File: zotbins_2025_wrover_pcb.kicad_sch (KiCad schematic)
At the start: 40 parts, among them J1 Conn_01x28_Pin, J2 DCJ200-10-A-XX-K_REVA, J3 HC-SR04_Screw_Terminal_01x04, J4 HX711_Screw_Terminal_01x05, J5 Main_Servo_Screw_Terminal_01x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, J6 Conn_01x30_Pin, J7 SG_Servo_Screw_Terminal_01x03, J8 BB_Receiver_Screw_Terminal_01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, J9 BB_Transmitter_Screw_Terminal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, U1 LM350_TO220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

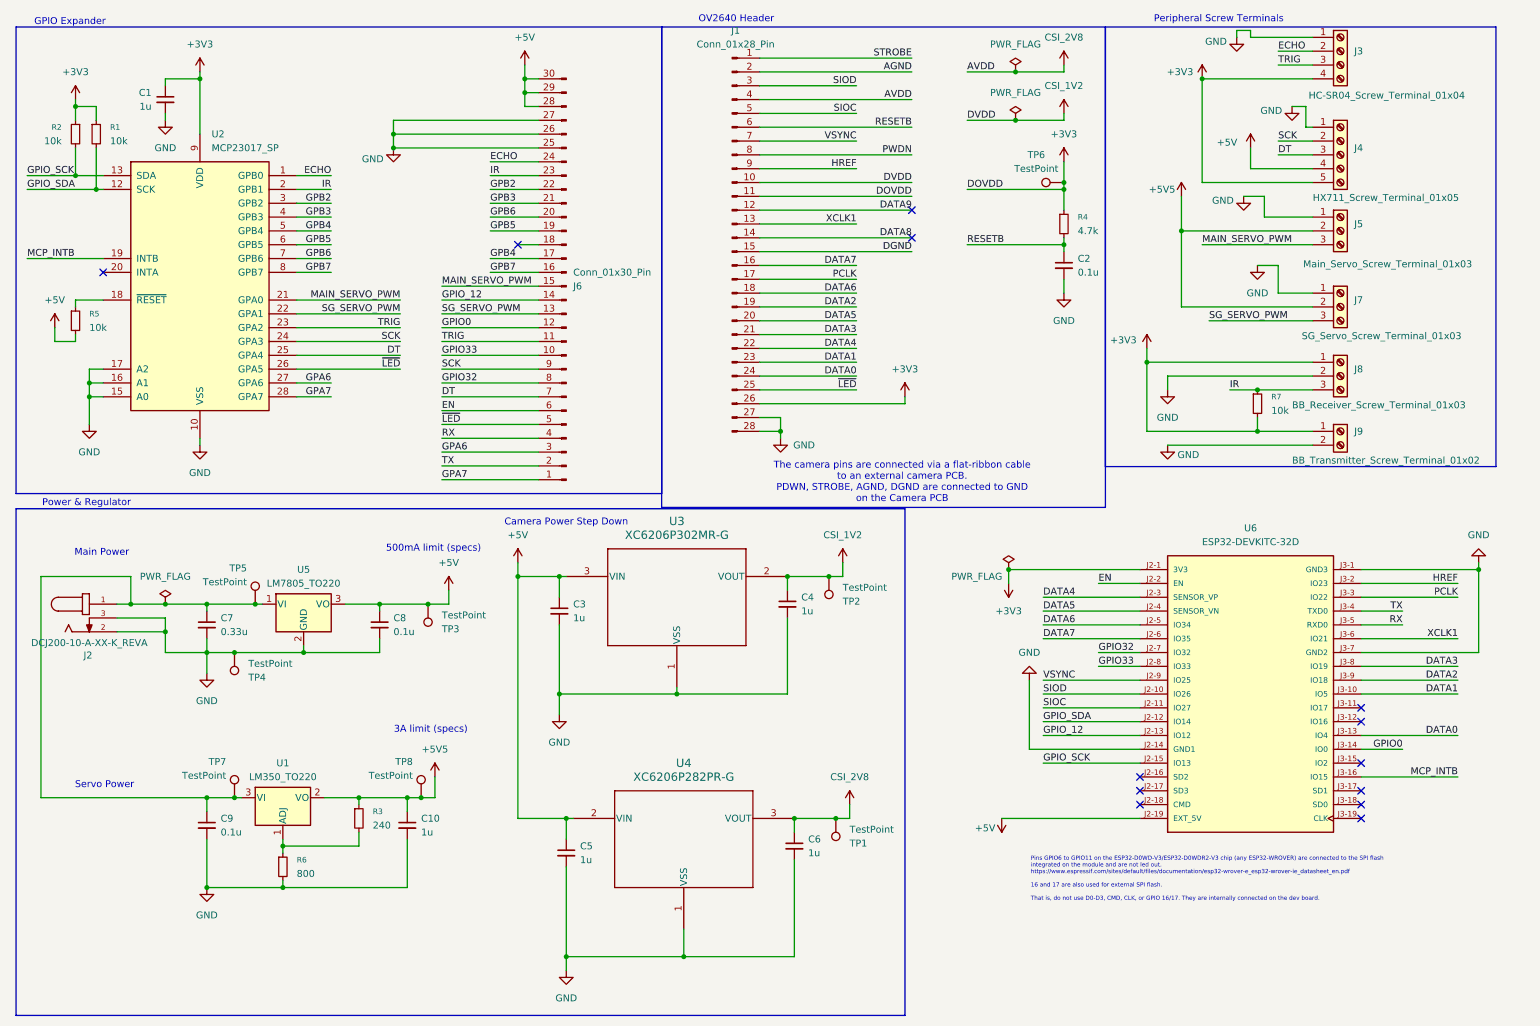
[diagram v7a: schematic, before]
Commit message: fixed net name ambiguity on schematic
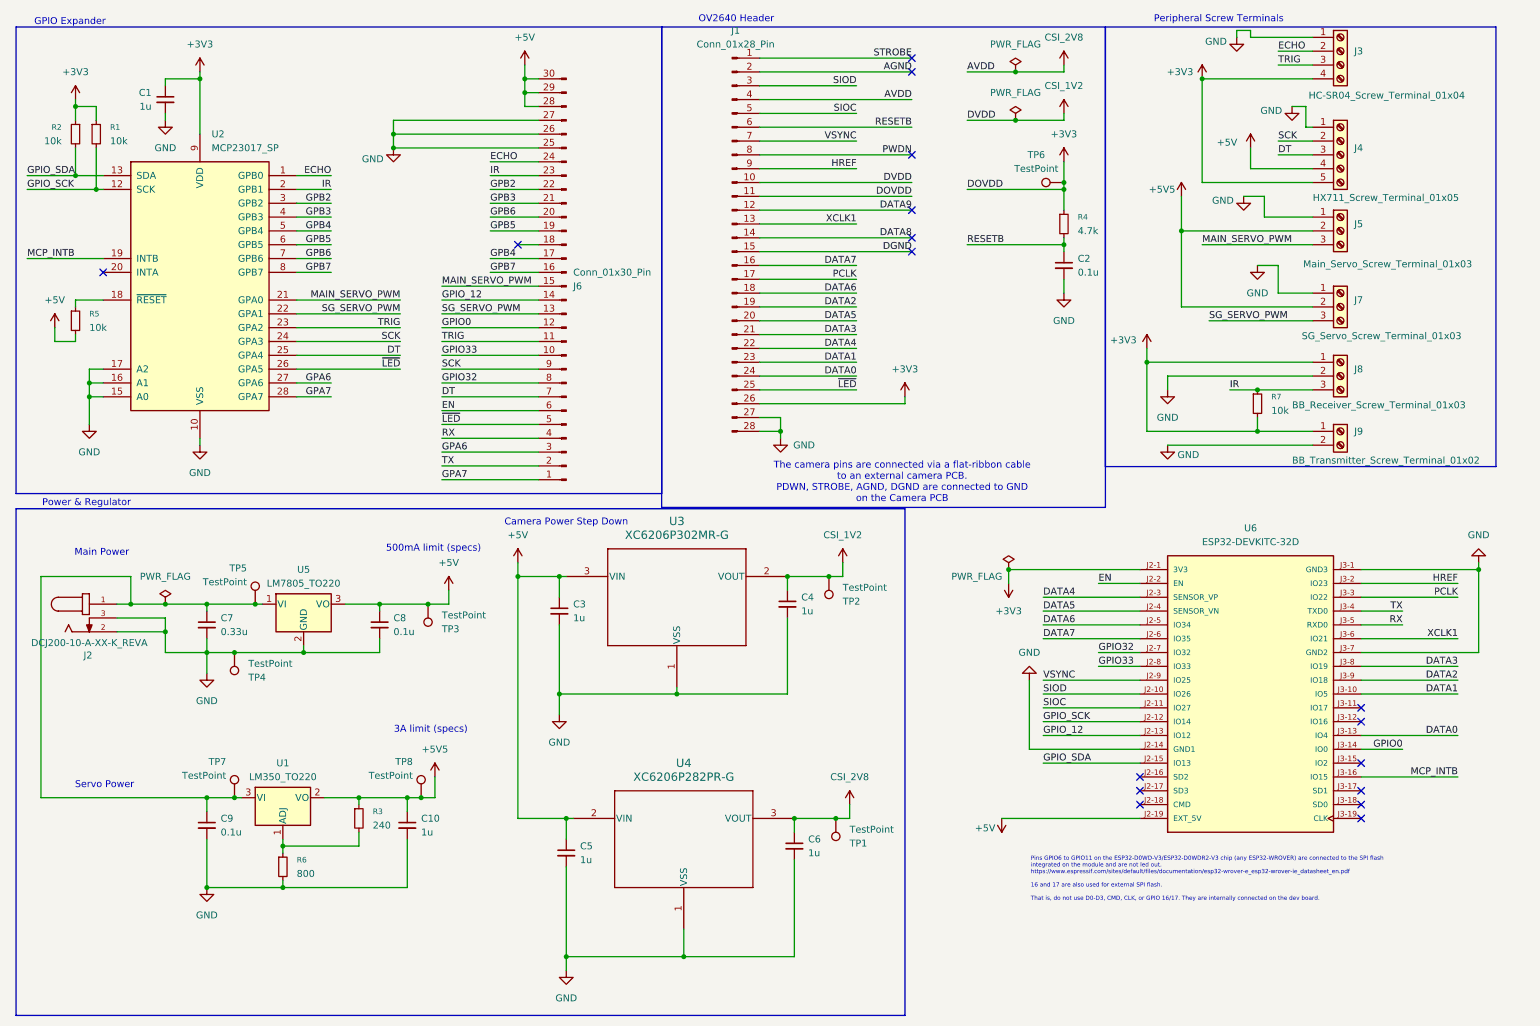
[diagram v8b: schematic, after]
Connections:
- net GPIO_SCK: now also R1.2, U2.12 (SCK), U6.J2-12 (IO14); no longer R2.2, U2.13 (SDA), U6.J2-15 (IO13)
- net GPIO_SDA: now also R2.2, U2.13 (SDA), U6.J2-15 (IO13); no longer R1.2, U2.12 (SCK), U6.J2-12 (IO14)
- no-connect marks 13 -> 17
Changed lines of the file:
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@@
 	)
 	(no_connect
+		(at 176.53 57.15)
+	)
+	(no_connect
 		(at 27.94 60.96)
 	)
@@
 	)
 	(no_connect
+		(at 176.53 39.37)
+	)
+	(no_connect
 		(at 104.14 55.88)
 	)
@@
 	)
 	(no_connect
+		(at 176.53 24.13)
+	)
+	(no_connect
 		(at 218.44 158.75)
 	)
@@
 	)
 	(no_connect
+		(at 176.53 21.59)
+	)
+	(no_connect
 		(at 259.08 143.51)
 	)
@@
 	)
 	(label "GPIO_SCK"
-		(at 13.97 43.18 0)
+		(at 13.97 45.72 0)
 		(effects
 			(font
@@
 	)
 	(label "GPIO_SDA"
-		(at 13.97 45.72 0)
+		(at 13.97 43.18 0)
 		(effects
 			(font
@@
 	)
 	(label "GPIO_SDA"
-		(at 200.66 143.51 0)
+		(at 200.66 151.13 0)
 		(effects
 			(font
@@
 	)
 	(label "GPIO_SCK"
-		(at 200.66 151.13 0)
+		(at 200.66 143.51 0)
 		(effects
 			(font
